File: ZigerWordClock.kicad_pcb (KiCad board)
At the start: 2 copper layers, 237 x 237 mm, 61 parts, among them J1 SAO 1.69bis, U1 BH1750, U10 BTF-5V-060L-B_SK9822_LED_Stri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, U11 BTF-5V-060L-B_SK9822_LED_Stri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, U12 BTF-5V-060L-B_SK9822_LED_Stri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, U13 BTF-5V-060L-B_SK9822_LED_Stri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, U14 BTF-5V-060L-B_SK9822_LED_Stri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, U15 BTF-5V-060L-B_SK9822_LED_Stri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, U16 BTF-5V-060L-B_SK9822_LED_Stri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, U17 BTF-5V-060L-B_SK9822_LED_Stri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, U18 BTF-5V-060L-B_SK9822_LED_Stri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, U19 BTF-5V-060L-B_SK9822_LED_Stri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, U2 LILYGO(R)_TTGO_T8_ESP32-S2_V1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, U20 IR-Module_38KHz, U3 BTF-5V-060L-B_SK9822_LED_Stri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, U4 LevelShifter, U5 BTF-5V-060L-B_SK9822_LED_Stri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, U6 BTF-5V-060L-B_SK9822_LED_Stri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, U7 BTF-5V-060L-B_SK9822_LED_Stri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, U8 BTF-5V-060L-B_SK9822_LED_Stri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, U9 BTF-5V-060L-B_SK9822_LED_Stri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

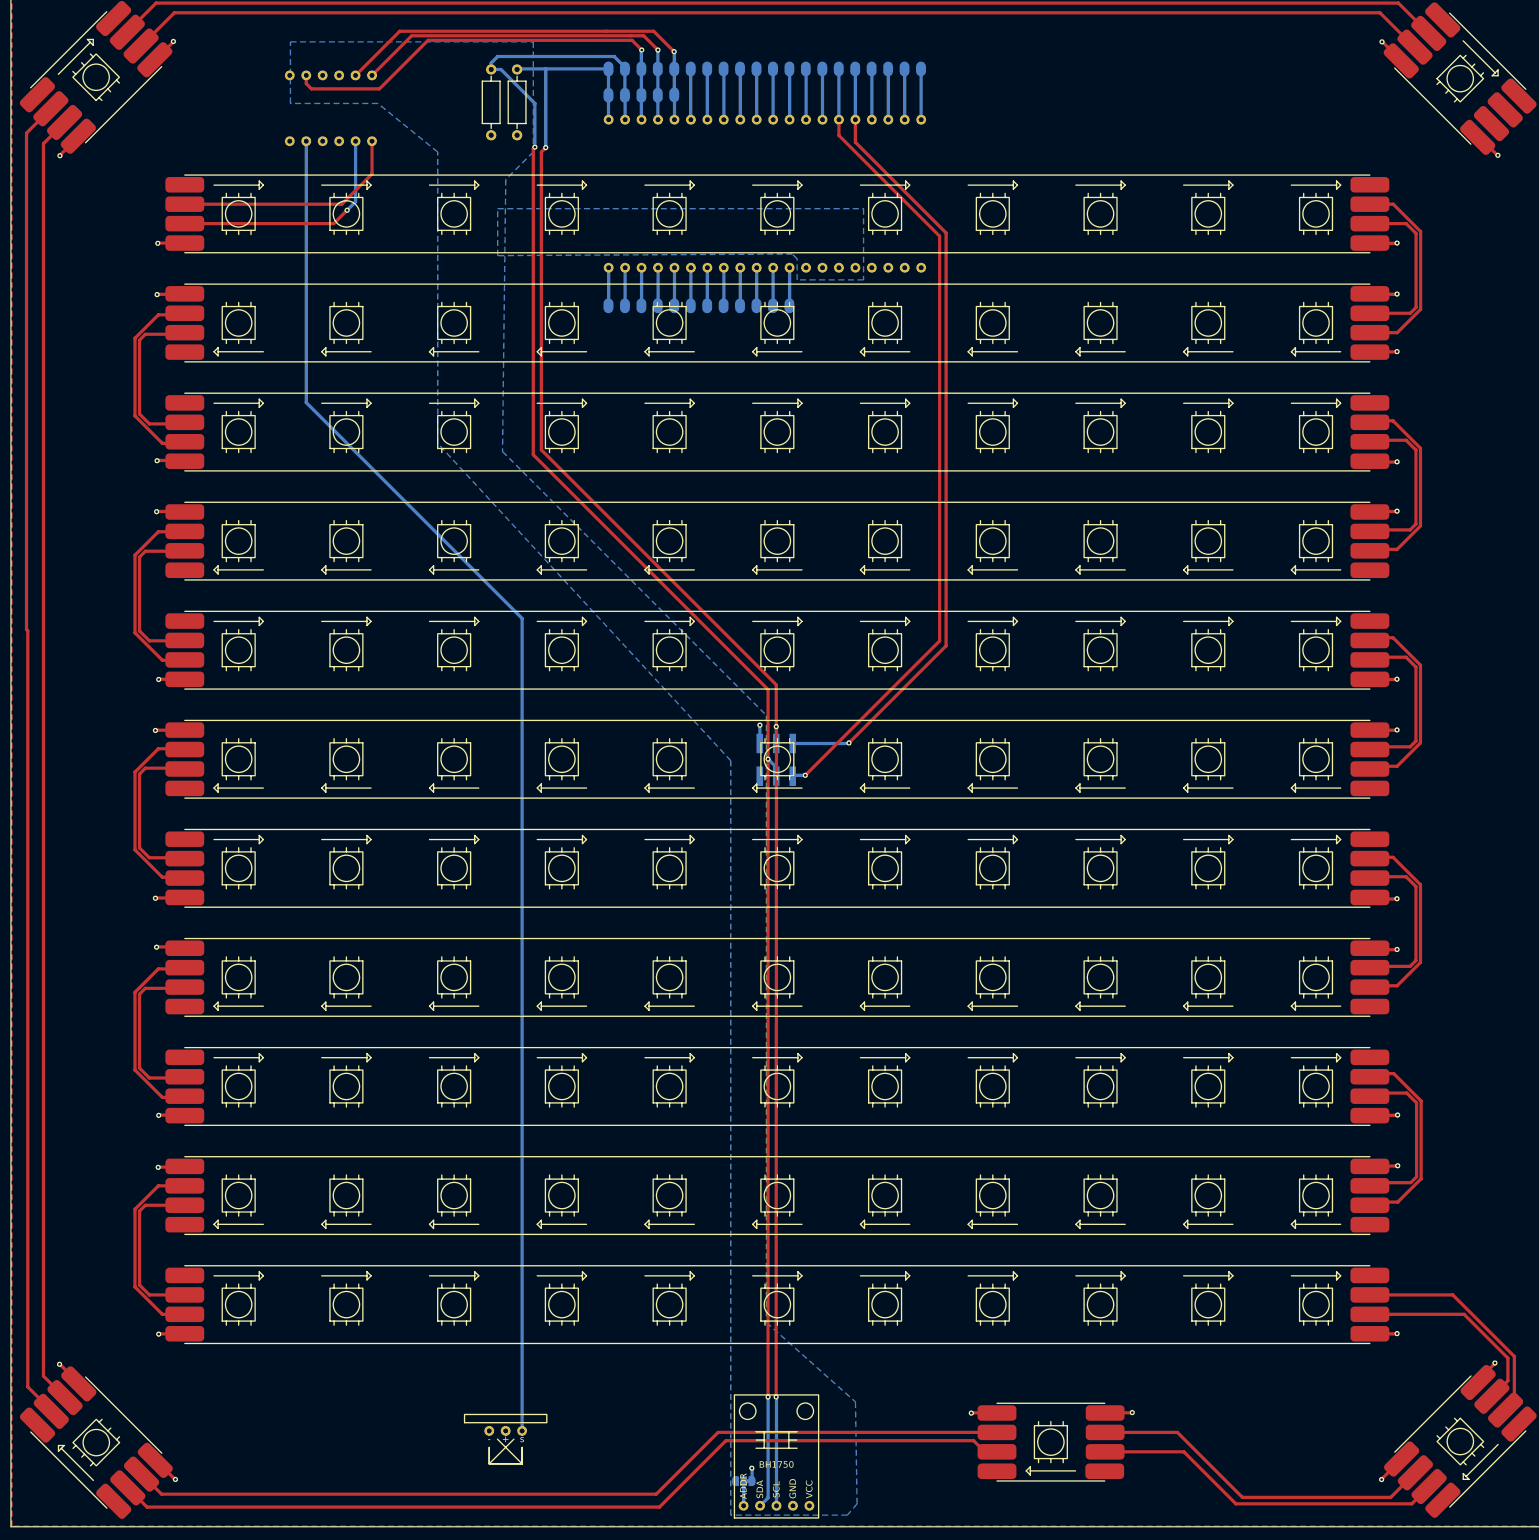
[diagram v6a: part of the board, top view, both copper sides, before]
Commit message: Pin labels added
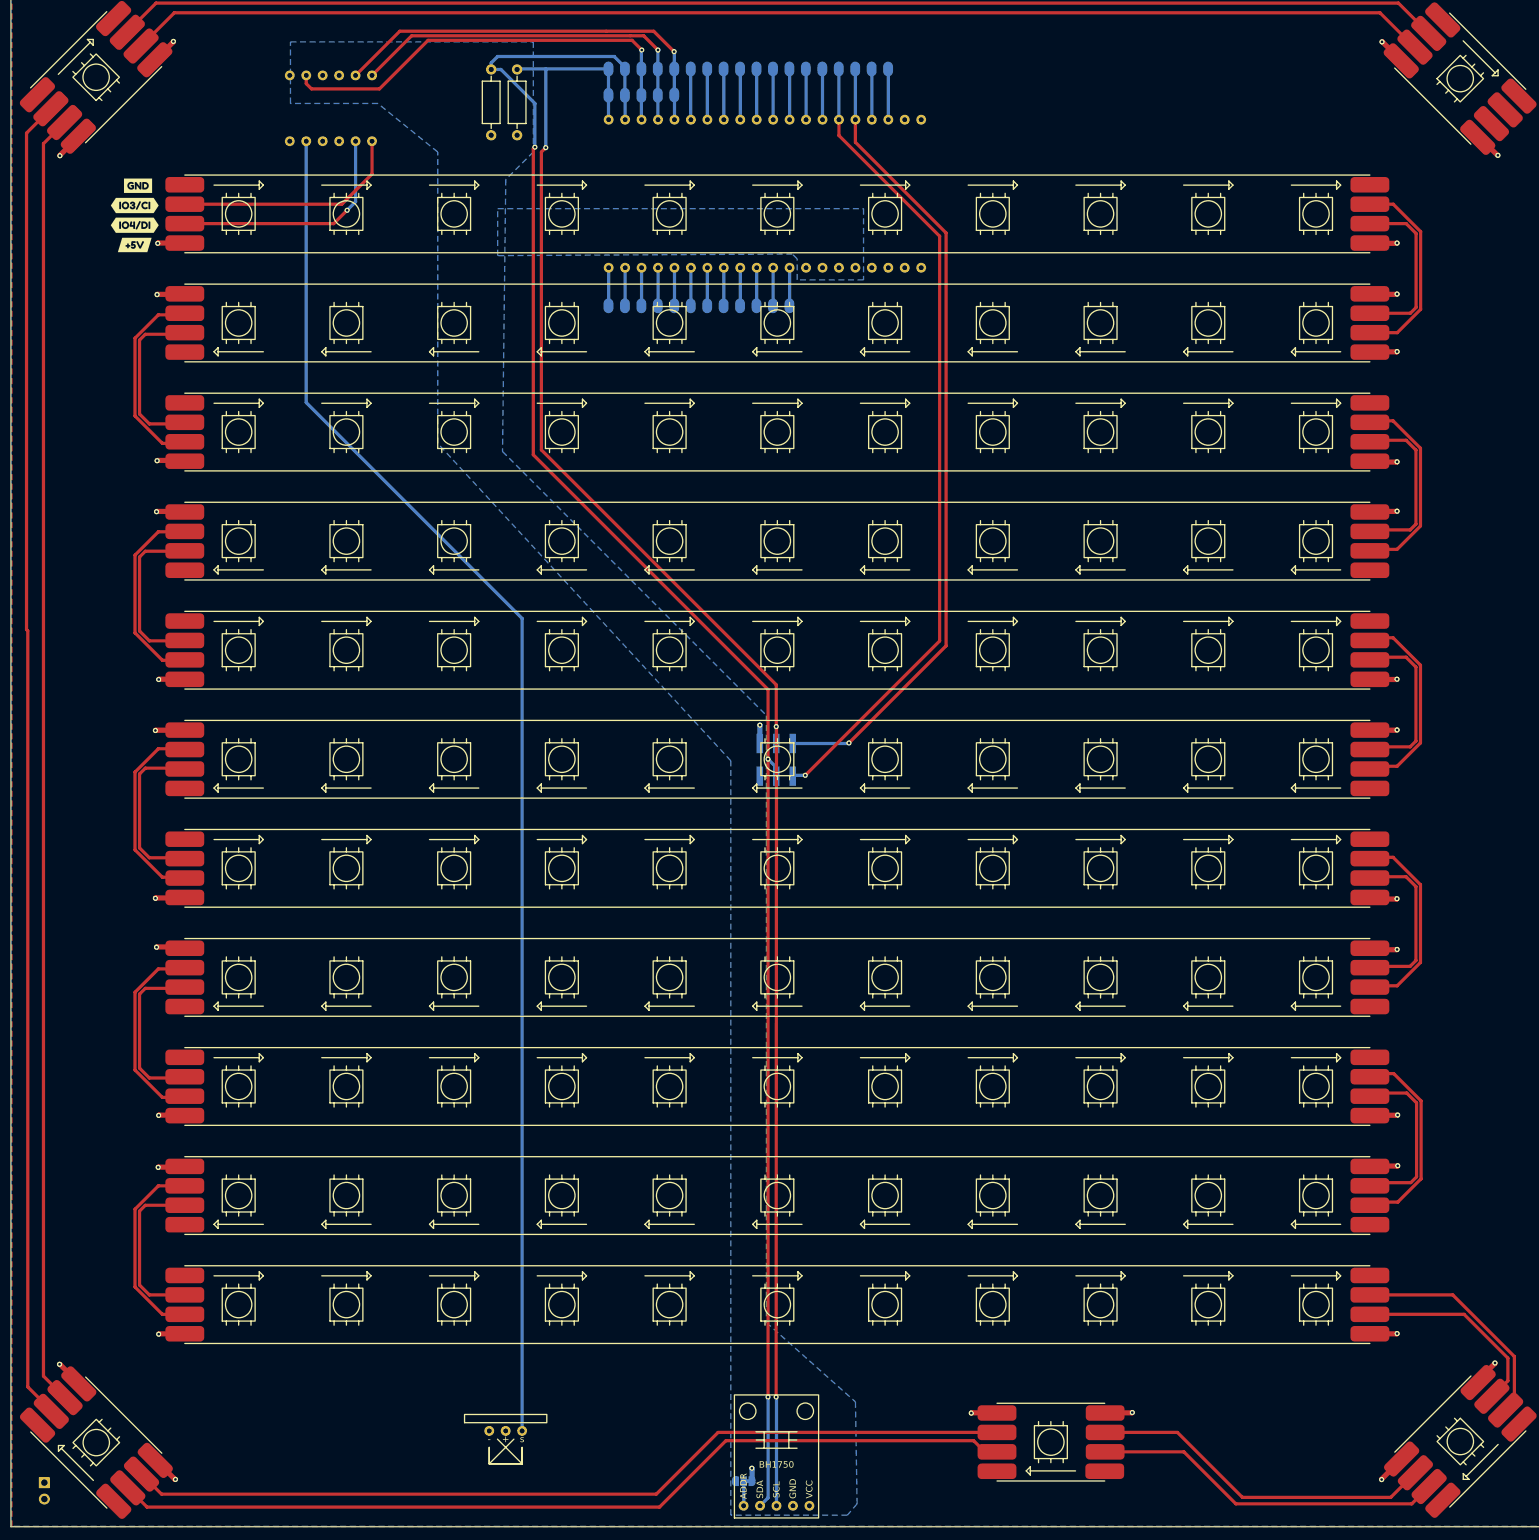
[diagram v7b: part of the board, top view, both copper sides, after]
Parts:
- removed JP25, JP26: Pad, WordClock Footprint Library:Pad
- added J2: Barrel_Jack, Connector_PinHeader_2.54mm:PinHeader_1x02_P2.54mm_Vertical, B.Cu at (47.0, 261.2)
- added kibuzzard-620DE71B: G***, kibuzzard-620DE71B, B.Cu at (134.1, 84.0)
- added kibuzzard-620DE782: G***, kibuzzard-620DE782, B.Cu at (136.7, 84.2)
- added kibuzzard-620DE80D: G***, kibuzzard-620DE80D, B.Cu at (157.0, 254.3)
- added kibuzzard-620DE80D: G***, kibuzzard-620DE80D, B.Cu at (160.0, 159.5)
- added kibuzzard-620DE80D: G***, kibuzzard-620DE80D, B.Cu at (134.1, 36.3)
- added kibuzzard-620DEA12: G***, kibuzzard-620DEA12, B.Cu at (160.0, 139.7)
- added kibuzzard-620DEA12: G***, kibuzzard-620DEA12, B.Cu at (136.7, 36.6)
- added kibuzzard-620DEA12: G***, kibuzzard-620DEA12, B.Cu at (159.5, 254.5)
- added kibuzzard-620DEA49: G***, kibuzzard-620DEA49, B.Cu at (120.9, 246.9)
- added kibuzzard-620DEA49: G***, kibuzzard-620DEA49, B.Cu at (139.2, 36.6)
- added kibuzzard-620DEA86: G***, kibuzzard-620DEA86, F.Cu at (61.0, 64.0)
- added kibuzzard-620DEA86: G***, kibuzzard-620DEA86, B.Cu at (141.7, 37.1)
- added kibuzzard-620DEAF9: G***, kibuzzard-620DEAF9, B.Cu at (157.0, 38.1)
- added kibuzzard-620DEB10: G***, kibuzzard-620DEB10, B.Cu at (159.5, 38.1)
- added kibuzzard-620DEB75: G***, kibuzzard-620DEB75, B.Cu at (169.7, 38.1)
- added kibuzzard-620DEB83: G***, kibuzzard-620DEB83, B.Cu at (172.2, 38.1)
- added kibuzzard-620DEBCF: G***, kibuzzard-620DEBCF, F.Cu at (61.0, 67.1)
- added kibuzzard-620DEBCF: G***, kibuzzard-620DEBCF, B.Cu at (144.3, 37.1)
- added kibuzzard-620DEC17: G***, kibuzzard-620DEC17, B.Cu at (174.8, 38.1)
- added kibuzzard-620DEC24: G***, kibuzzard-620DEC24, B.Cu at (177.3, 38.1)
- added kibuzzard-620DECE9: G***, kibuzzard-620DECE9, B.Cu at (146.8, 38.1)
- added kibuzzard-620DED0B: G***, kibuzzard-620DED0B, B.Cu at (149.4, 38.1)
- added kibuzzard-620DED15: G***, kibuzzard-620DED15, B.Cu at (151.9, 38.1)
- added kibuzzard-620DED33: G***, kibuzzard-620DED33, B.Cu at (154.4, 38.1)
- added kibuzzard-620DED42: G***, kibuzzard-620DED42, B.Cu at (162.1, 38.1)
- added kibuzzard-620DED4F: G***, kibuzzard-620DED4F, B.Cu at (164.6, 38.1)
- added kibuzzard-620DED59: G***, kibuzzard-620DED59, B.Cu at (167.1, 37.6)
- added kibuzzard-620DEDB9: G***, kibuzzard-620DEDB9, B.Cu at (162.6, 138.7)
- added kibuzzard-620DEDD7: G***, kibuzzard-620DEDD7, B.Cu at (162.6, 160.5)
- added kibuzzard-620DEFD1: G***, kibuzzard-620DEFD1, F.Cu at (61.0, 70.1)
- added kibuzzard-620DEFD1: G***, kibuzzard-620DEFD1, B.Cu at (118.4, 247.4)
- added kibuzzard-620DEFD1: G***, kibuzzard-620DEFD1, B.Cu at (179.8, 79.8)
- added kibuzzard-620DEFD1: G***, kibuzzard-620DEFD1, B.Cu at (89.9, 58.9)
- added kibuzzard-620DEFD1: G***, kibuzzard-620DEFD1, B.Cu at (182.4, 79.8)
- added kibuzzard-620DF03F: G***, kibuzzard-620DF03F, B.Cu at (165.1, 255.5)
- added kibuzzard-620DF03F: G***, kibuzzard-620DF03F, B.Cu at (157.5, 158.0)
- added kibuzzard-620DF03F: G***, kibuzzard-620DF03F, B.Cu at (89.9, 39.1)
- added kibuzzard-620DF0B9: G***, kibuzzard-620DF0B9, F.Cu at (61.5, 61.0)
- added kibuzzard-620DF0B9: G***, kibuzzard-620DF0B9, B.Cu at (92.5, 39.6)
- added kibuzzard-620DF0B9: G***, kibuzzard-620DF0B9, B.Cu at (162.1, 256.0)
- added kibuzzard-620DF0B9: G***, kibuzzard-620DF0B9, B.Cu at (177.3, 79.8)
- added kibuzzard-620DF0B9: G***, kibuzzard-620DF0B9, B.Cu at (93.0, 58.9)
- added kibuzzard-620DF0B9: G***, kibuzzard-620DF0B9, B.Cu at (169.7, 79.8)
- added kibuzzard-620DF0B9: G***, kibuzzard-620DF0B9, B.Cu at (157.0, 140.7)
- added kibuzzard-620DF0B9: G***, kibuzzard-620DF0B9, B.Cu at (174.8, 79.8)
- added kibuzzard-620DF0B9: G***, kibuzzard-620DF0B9, B.Cu at (115.8, 247.9)
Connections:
- U2 pad 19: Net-(JP25-Pad1) -> unconnected-(U2-Pad19)
- U2 pad 20: Net-(JP26-Pad1) -> unconnected-(U2-Pad20)
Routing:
- net Net-(JP25-Pad1): track 7.85 -> 0.00 mm
- net Net-(JP26-Pad1): track 7.85 -> 0.00 mm
